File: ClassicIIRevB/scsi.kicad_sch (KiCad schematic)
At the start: 12 parts, among them J4 EXT SCSI, J8 INT SCSI, U8 Am85C80

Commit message: improved footprints and silkscreens
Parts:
- U8: footprint Package_LCC:PLCC-68_24.2x24.2mm_P1.27mm -> MyPackage:PLCC-68_24.2x24.2mm_P1.27mm_oval
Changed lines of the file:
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@@
 	(title_block
 		(title "Macintosh Classic II Revision B")
-		(date "2025-05-31")
+		(date "2025-06-04")
 		(company "Apple Computer")
 		(comment 1 "drawn by Bradley Bell")
@@
 			)
 		)
-		(property "Footprint" "Package_LCC:PLCC-68_24.2x24.2mm_P1.27mm"
+		(property "Footprint" "MyPackage:PLCC-68_24.2x24.2mm_P1.27mm_oval"
 			(at 168.91 173.99 0)
 			(effects
@@
 			)
 		)
-		(property "Footprint" "Package_LCC:PLCC-68_24.2x24.2mm_P1.27mm"
+		(property "Footprint" "MyPackage:PLCC-68_24.2x24.2mm_P1.27mm_oval"
 			(at 69.85 102.87 0)
 			(effects

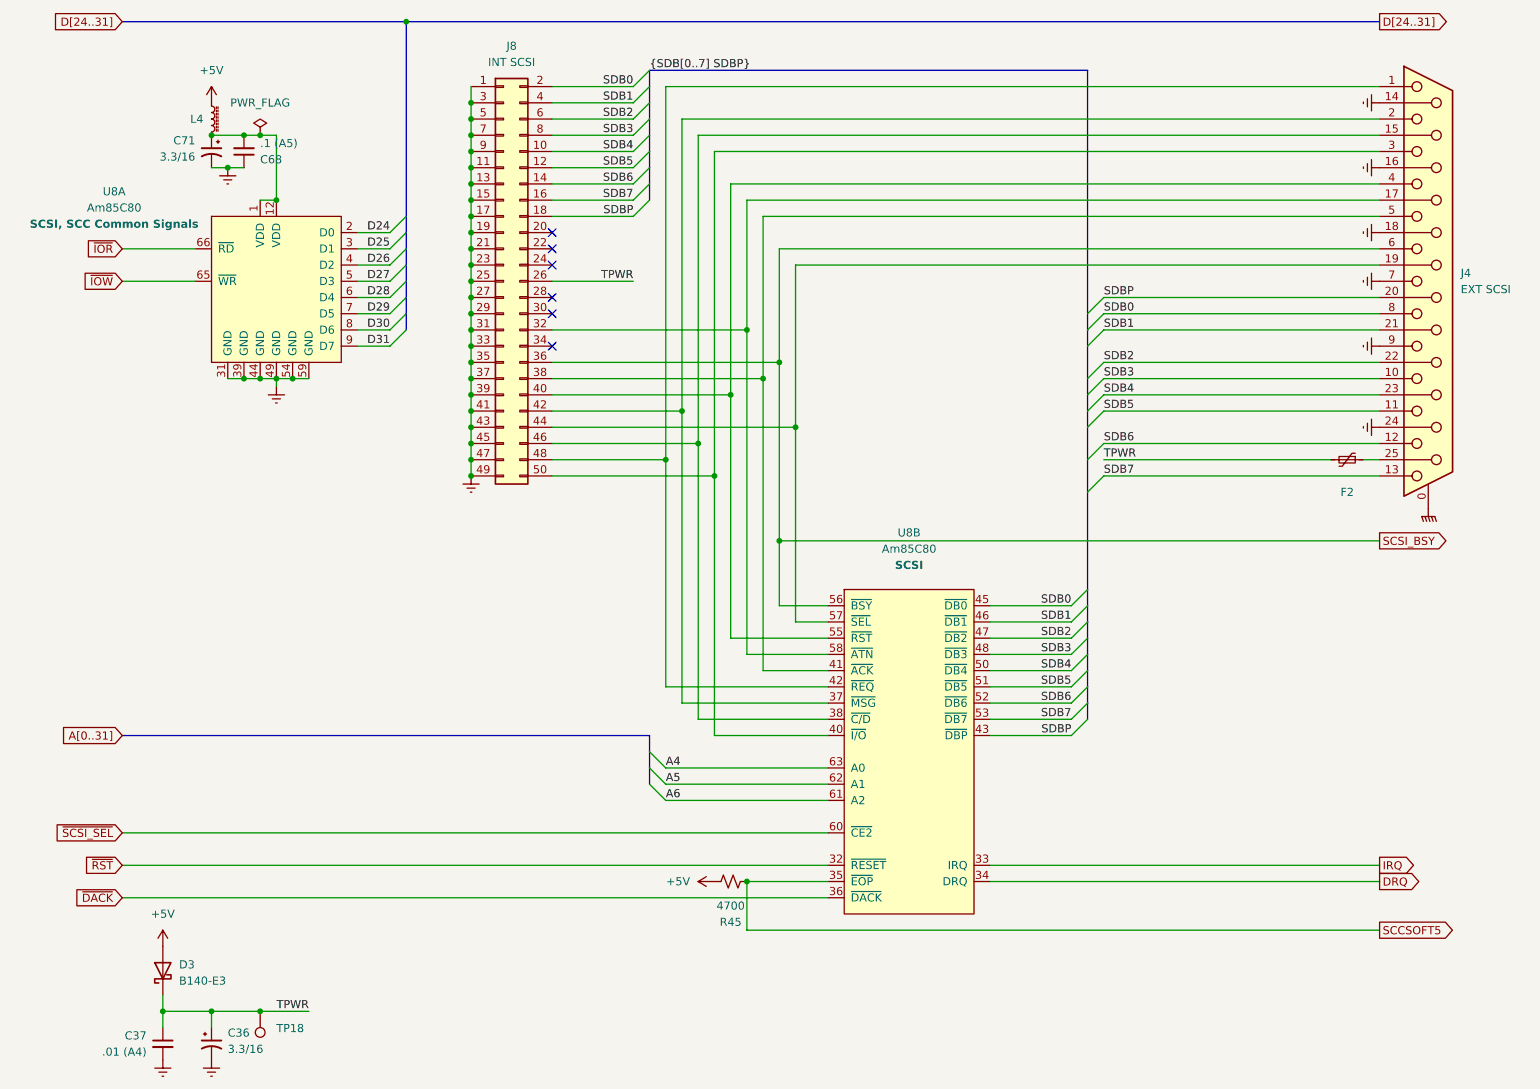
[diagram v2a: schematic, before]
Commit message: Switch to some "official" net names
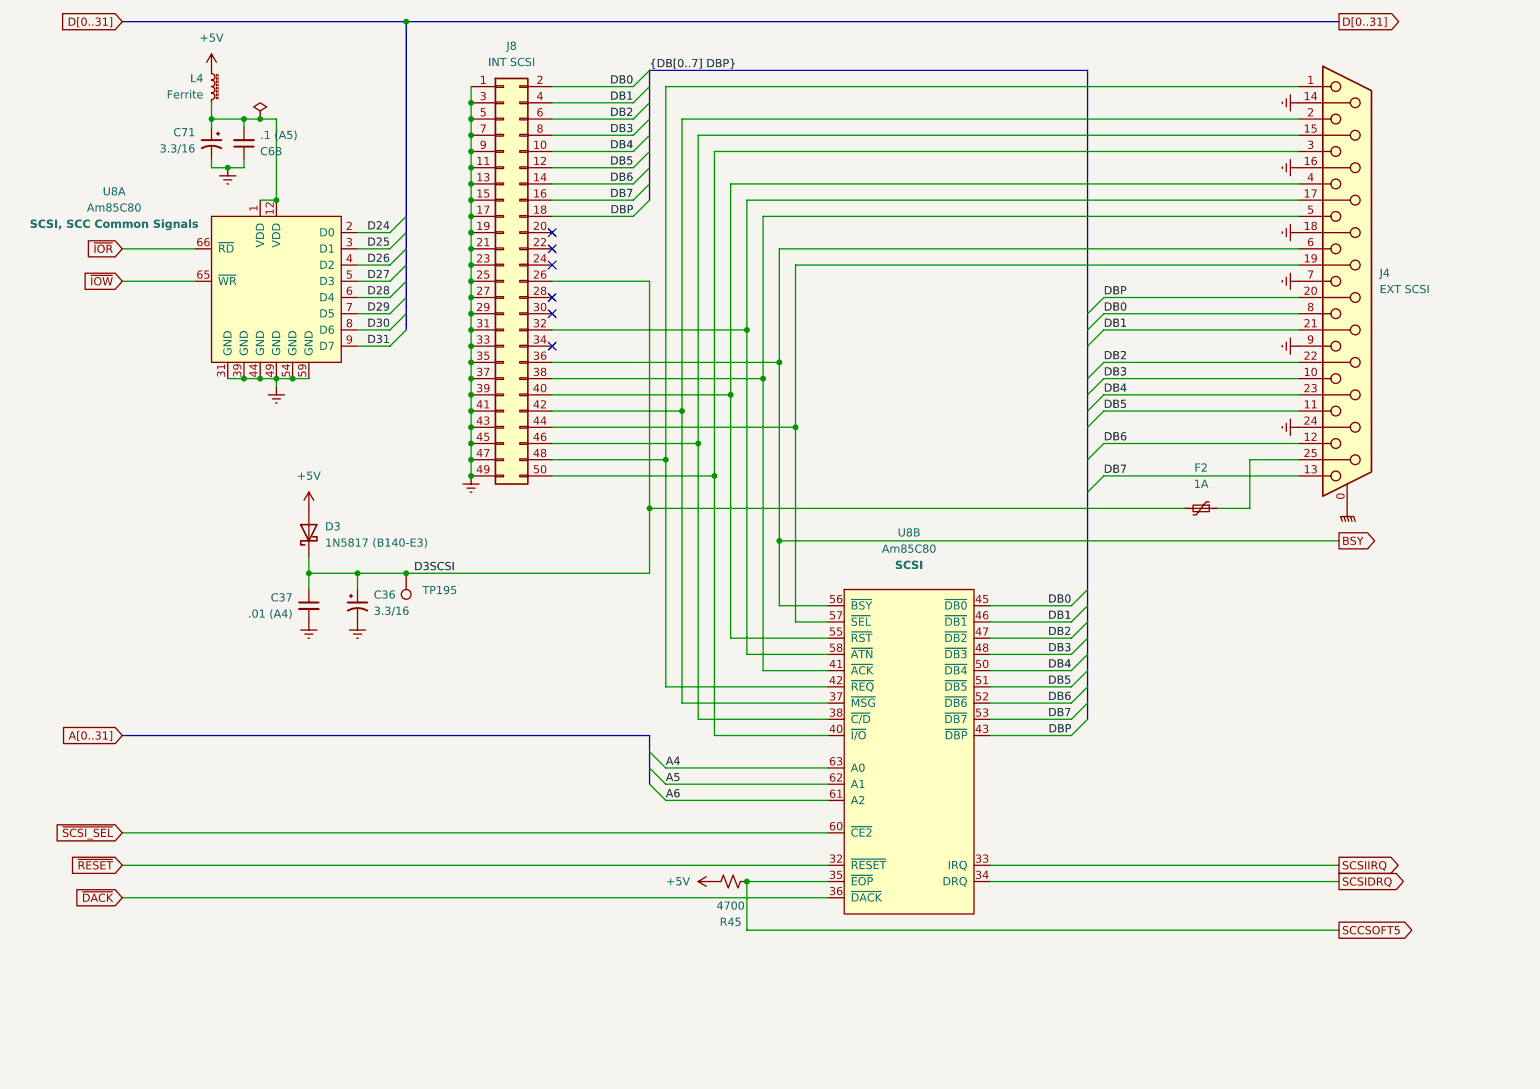
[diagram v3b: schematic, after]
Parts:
- D3: value B140-E3 -> 1N5817 (B140-E3)
- F2: value Polyfuse_Small -> 1A
- L4: value L_Ferrite_Small -> Ferrite
- renumbered TP18 to TP195
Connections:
- net DRQ renamed SCSIDRQ
- net IRQ renamed SCSIIRQ
- net SCSI_BSY renamed BSY
- net SDB0 renamed DB0
- net SDB1 renamed DB1
- net SDB2 renamed DB2
- net SDB3 renamed DB3
- net SDB4 renamed DB4
- net SDB5 renamed DB5
- net SDB6 renamed DB6
- net SDB7 renamed DB7
- net SDBP renamed DBP
- net TPWR renamed D3SCSI
- net ~{RST} renamed ~{RESET}
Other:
- moved on the sheet: C36, C37, C68, C71, D3, F2, J4, L4, TP195

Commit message: update exports
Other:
- title: Macintosh Classic II Revision B -> Macintosh Classic II (Later Revision)
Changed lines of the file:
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@@
 	(paper "USLetter")
 	(title_block
-		(title "Macintosh Classic II Revision B")
-		(date "2025-06-04")
+		(title "Macintosh Classic II (Later Revision)")
+		(date "2025-06-16")
 		(company "Apple Computer")
 		(comment 1 "drawn by Bradley Bell")

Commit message: Corrections to SMDs, more improved footprints
The later revision board reproduction design is now complete.
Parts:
- C36, C71: value 3.3/16 -> 3.3uF 16V
- C37: value .01 (A4) -> 10nF
- C68: value .1 (A5) -> 100nF
- D3: value 1N5817 (B140-E3) -> 1N5817; PartNum (none) -> B140-E3
- J4: footprint Connector_Dsub:DSUB-25_Socket_Horizontal_P2.77x2.84mm_EdgePinOffset7.70mm_Housed_MountingHolesOffset9.12mm -> Connector_Mine:DSUB-25_Socket_Horizontal_P2.77x2.84mm_EdgePinOffset7.70mm_Housed_MountingHolesOffset9.12mm
- J8: footprint Connector_IDC:IDC-Header_2x25_P2.54mm_Vertical -> Connector_Mine:IDC-Header_2x25_P2.54mm_Vertical
- R45: value 4700 -> 4.7K
- TP195: now left out of the parts list
- U8: value Am85C80 -> AM85C80; PartNum (none) -> 337S8580
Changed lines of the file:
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@@
 	(title_block
 		(title "Macintosh Classic II (Later Revision)")
-		(date "2025-06-16")
+		(date "2025-06-21")
 		(company "Apple Computer")
 		(comment 1 "drawn by Bradley Bell")
@@
 	)
 	(junction
-		(at 142.24 160.02)
-		(diameter 0)
-		(color 0 0 0 0)
-	)
-	(junction
 		(at 99.06 53.34)
 		(diameter 0)
@@
 	)
 	(junction
+		(at 144.78 160.02)
+		(diameter 0)
+		(color 0 0 0 0)
+	)
+	(junction
 		(at 149.86 88.9)
 		(diameter 0)
@@
 	(wire
 		(pts
-			(xy 142.24 160.02) (xy 154.94 160.02)
+			(xy 142.24 160.02) (xy 144.78 160.02)
 		)
 		(stroke
@@
 	(wire
 		(pts
-			(xy 142.24 167.64) (xy 234.95 167.64)
+			(xy 144.78 167.64) (xy 234.95 167.64)
 		)
 		(stroke
@@
 	(wire
 		(pts
-			(xy 142.24 160.02) (xy 142.24 167.64)
+			(xy 144.78 160.02) (xy 144.78 167.64)
 		)
 		(stroke
@@
 	(wire
 		(pts
+			(xy 144.78 160.02) (xy 154.94 160.02)
+		)
+		(stroke
+			(width 0)
+			(type default)
+		)
+	)
+	(wire
+		(pts
 			(xy 134.62 91.44) (xy 111.76 91.44)
 		)
@@
 			)
 		)
-		(property "Value" ".01 (A4)"
+		(property "Value" "10nF"
 			(at 71.12 118.1162 0)
 			(effects
@@
 		)
 		(property "Value" "EXT SCSI"
-			(at 241.3 67.3099 0)
+			(at 241.3 67.31 0)
 			(effects
 				(font
 					(size 1.27 1.27)
+					(thickness 0.254)
+					(bold yes)
 				)
 				(justify left)
 			)
 		)
-		(property "Footprint" "Connector_Dsub:DSUB-25_Socket_Horizontal_P2.77x2.84mm_EdgePinOffset7.70mm_Housed_MountingHolesOffset9.12mm"
+		(property "Footprint" "Connector_Mine:DSUB-25_Socket_Horizontal_P2.77x2.84mm_EdgePinOffset7.70mm_Housed_MountingHolesOffset9.12mm"
 			(at 236.22 66.04 0)
 			(effects
@@
 			)
 		)
-		(property "Value" "3.3/16"
+		(property "Value" "3.3uF 16V"
 			(at 83.82 117.6781 0)
 			(effects
@@
 			)
 		)
-		(property "Value" "4700"
+		(property "Value" "4.7K"
 			(at 139.7 163.83 90)
 			(effects
@@
 		(fields_autoplaced yes)
 		(property "Reference" "U8"
-			(at 167.64 105.41 0)
+			(at 167.64 102.87 0)
 			(effects
 				(font
@@
 			)
 		)
-		(property "Value" "Am85C80"
-			(at 167.64 107.95 0)
+		(property "Value" "AM85C80"
+			(at 167.64 105.41 0)
 			(effects
 				(font
@@
 		)
 		(property "Desc2" "SCSI"
-			(at 167.64 110.49 0)
+			(at 167.64 107.95 0)
 			(effects
 				(font
@@
 			)
 		)
+		(property "PartNum" "337S8580"
+			(at 167.64 110.49 0)
+			(effects
+				(font
+					(size 1.27 1.27)
+				)
+			)
+		)
 		(pin "8"
 		)
@@
 		(fields_autoplaced yes)
 		(property "Reference" "D3"
-			(at 76.2 104.4574 90)
+			(at 76.2 103.1874 90)
 			(effects
 				(font
@@
 			)
 		)
-		(property "Value" "1N5817 (B140-E3)"
-			(at 76.2 106.9974 90)
+		(property "Value" "1N5817"
+			(at 76.2 105.7274 90)
 			(effects
 				(font
@@
 			)
 		)
+		(property "PartNum" "B140-E3"
+			(at 76.2 108.2674 90)
+			(effects
+				(font
+					(size 1.27 1.27)
+				)
+				(justify right)
+			)
+		)
 		(pin "2"
 		)
@@
 			)
 		)
-		(property "Value" "3.3/16"
+		(property "Value" "3.3uF 16V"
 			(at 55.88 45.2881 0)
 			(effects
@@
 		(fields_autoplaced yes)
 		(property "Reference" "U8"
-			(at 43.18 51.9998 0)
+			(at 43.18 49.4598 0)
 			(effects
 				(font
@@
 			)
 		)
-		(property "Value" "Am85C80"
-			(at 43.18 54.5398 0)
+		(property "Value" "AM85C80"
+			(at 43.18 51.9998 0)
 			(effects
 				(font
@@
 		)
 		(property "Description" "SCSI, SCC Common Signals"
-			(at 43.18 57.0799 0)
+			(at 43.18 54.5399 0)
 			(effects
 				(font
@@
 			)
 		)
+		(property "PartNum" "337S8580"
+			(at 43.18 57.0798 0)
+			(effects
+				(font
+					(size 1.27 1.27)
+				)
+			)
+		)
 		(pin "8"
 		)
@@
 			)
 		)
-		(property "Value" ".1 (A5)"
+		(property "Value" "100nF"
 			(at 66.04 43.1738 0)
 			(effects
@@
 				(font
 					(size 1.27 1.27)
+					(thickness 0.254)
+					(bold yes)
 				)
 			)
 		)
-		(property "Footprint" "Connector_IDC:IDC-Header_2x25_P2.54mm_Vertical"
+		(property "Footprint" "Connector_Mine:IDC-Header_2x25_P2.54mm_Vertical"
 			(at 104.14 66.04 0)
 			(effects
@@
 		(unit 1)
 		(exclude_from_sim no)
-		(in_bom yes)
+		(in_bom no)
 		(on_board yes)
 		(dnp no)
